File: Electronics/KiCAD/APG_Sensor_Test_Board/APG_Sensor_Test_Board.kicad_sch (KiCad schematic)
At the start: 0 parts

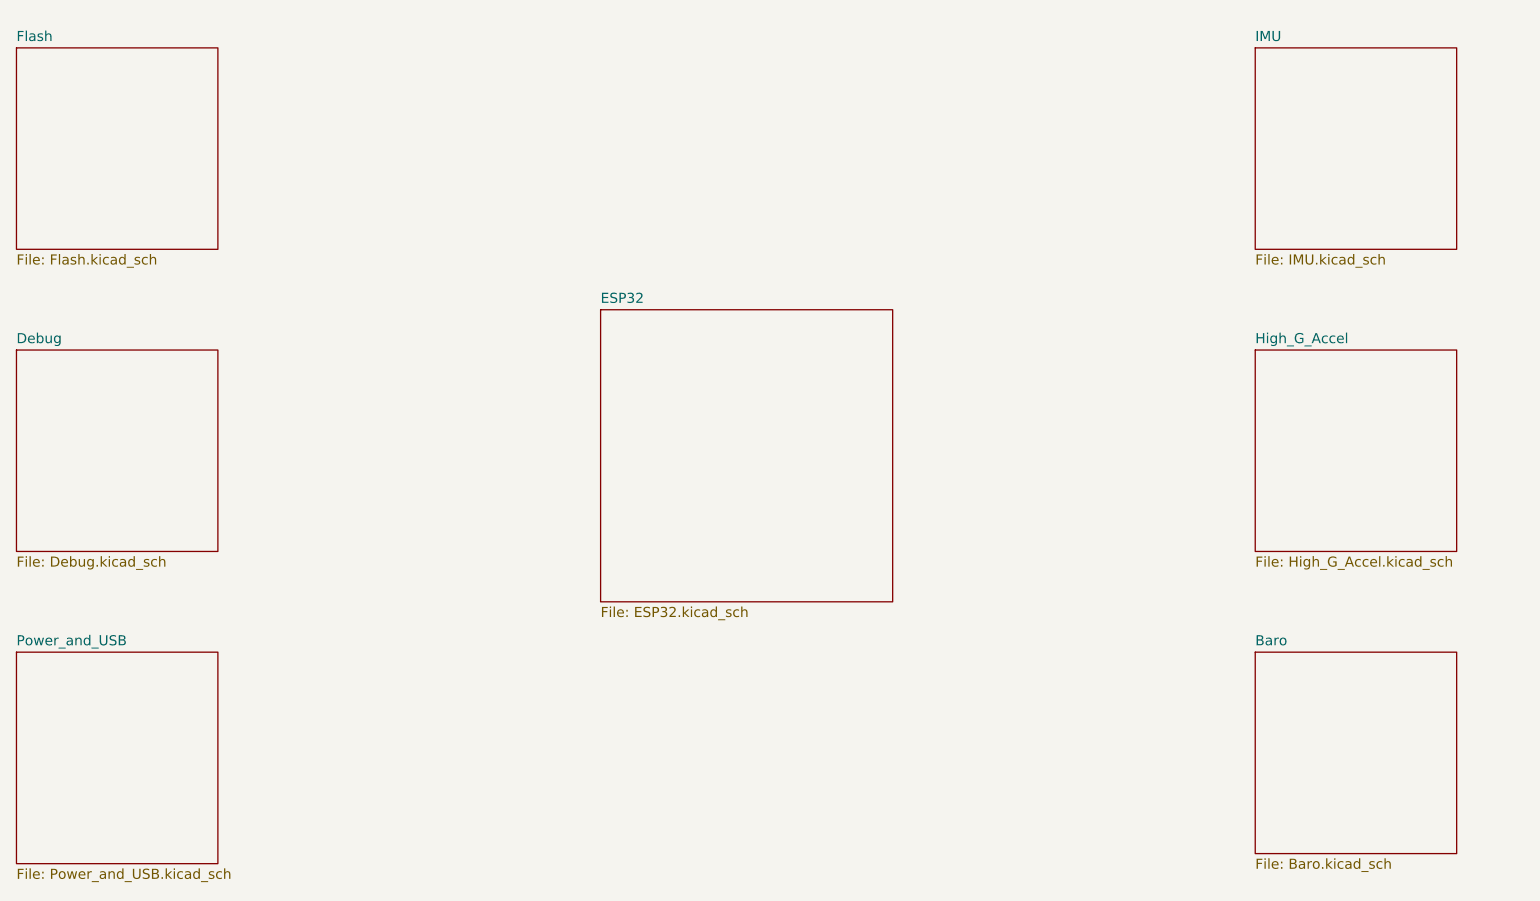
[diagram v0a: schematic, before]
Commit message: Gannon inspection decision to change IMU
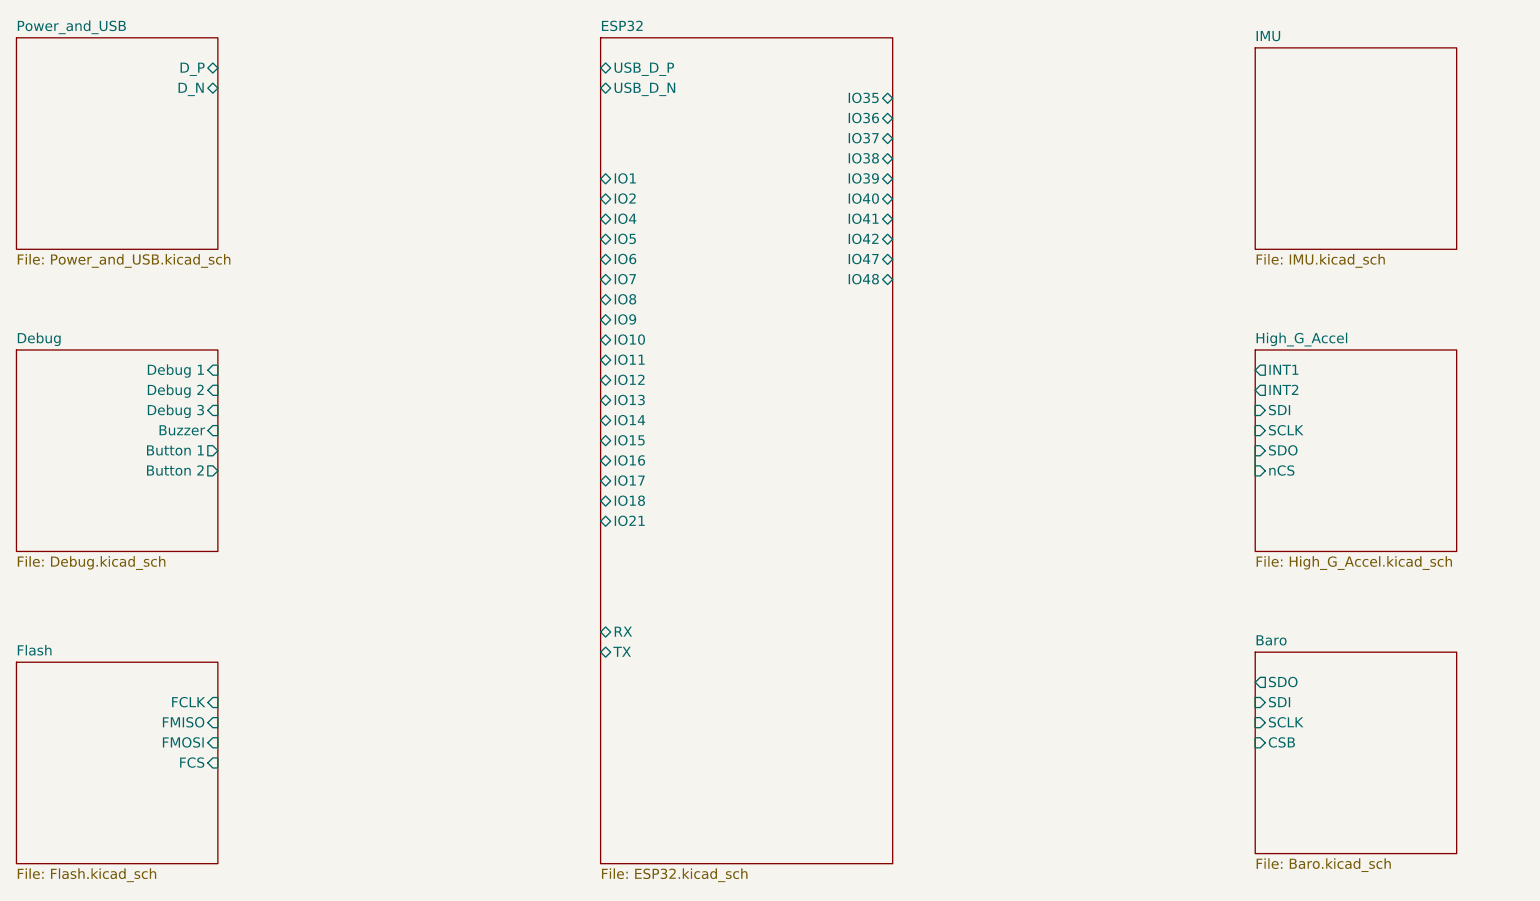
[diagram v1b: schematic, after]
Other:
- sheet Baro ports: added CSB, SCLK, SDI, SDO; removed none
- sheet Debug ports: added Button 1, Button 2, Buzzer, Debug 1, Debug 2, Debug 3; removed none
- sheet ESP32 ports: added IO1, IO10, IO11, IO12, IO13, IO14, IO15, IO16, IO17, IO18, IO2, IO21, IO35, IO36, IO37, IO38, IO39, IO4, IO40, IO41, IO42, IO47, IO48, IO5, IO6, IO7, IO8, IO9, RX, TX, USB_D_N, USB_D_P; removed none
- sheet Flash ports: added FCLK, FCS, FMISO, FMOSI; removed none
- sheet High_G_Accel ports: added INT1, INT2, SCLK, SDI, SDO, nCS; removed none
- sheet Power_and_USB ports: added D_N, D_P; removed none
